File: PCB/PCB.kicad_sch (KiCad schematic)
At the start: 14 parts, among them P1 SEN-11574, SW1 SW_Push, SW2 SW_Push, SW3 SW_Push, U1 TinyS3_Symbol, U2 ADXL343, U3 ST7789V

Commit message: Custom footprints and sch update with footprints
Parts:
- removed C2: 0.1u, symbol Device:C
- removed SW1, SW2, SW3: SW_Push, symbol Switch:SW_Push
- added R4, R5, R6, R7, R8: 220, Resistor_SMD:R_0402_1005Metric_Pad0.72x0.64mm_HandSolder, symbol Device:R
- added U4: switch3, symbol custom:switch3
- BT1: value LiPO 3.7V 1200 mAh -> LiPO 3.7V 1200 mAh
- C1, C3: footprint (none) -> Capacitor_SMD:C_0402_1005Metric_Pad0.74x0.62mm_HandSolder
- P1: footprint SEN-11574:XDCR_SEN-11574 -> footprints:Heart_headers
- R1, R2, R3: footprint (none) -> Resistor_SMD:R_0402_1005Metric_Pad0.72x0.64mm_HandSolder
- U1: footprint (none) -> footprints:TinyS3D_headers
- U2: footprint Package_LGA:LGA-14_3x5mm_P0.8mm_LayoutBorder1x6y -> footprints:ADXL345_header
- U3: footprint (none) -> footprints:LCD_header
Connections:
- net BTN1: now also U4. (BTN3)
- net BTN2: now also U4. (BTN3)
- net BTN3: now also U4. (BTN3)
- net CLK: now also R5.1; no longer U3. (VCC)
- net CS: now also R6.1; no longer U3. (VCC)
- net DC: now also R7.1; no longer U3. (VCC)
- net DIN: now also R4.1; no longer U3. (VCC)
- net GND: now also U1.2 (GND), U4. (BTN3)
- net RST: now also R8.1; no longer U3. (VCC)
- new net: R7.2, U3. (GND)
- new net: R8.2, U3. (GND)
- new net: R6.2, U3. (GND)
- new net: R4.2, U3. (GND)
- new net: R5.2, U3. (GND)
- no-connect marks 15 -> 14
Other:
- moved on the sheet: U1

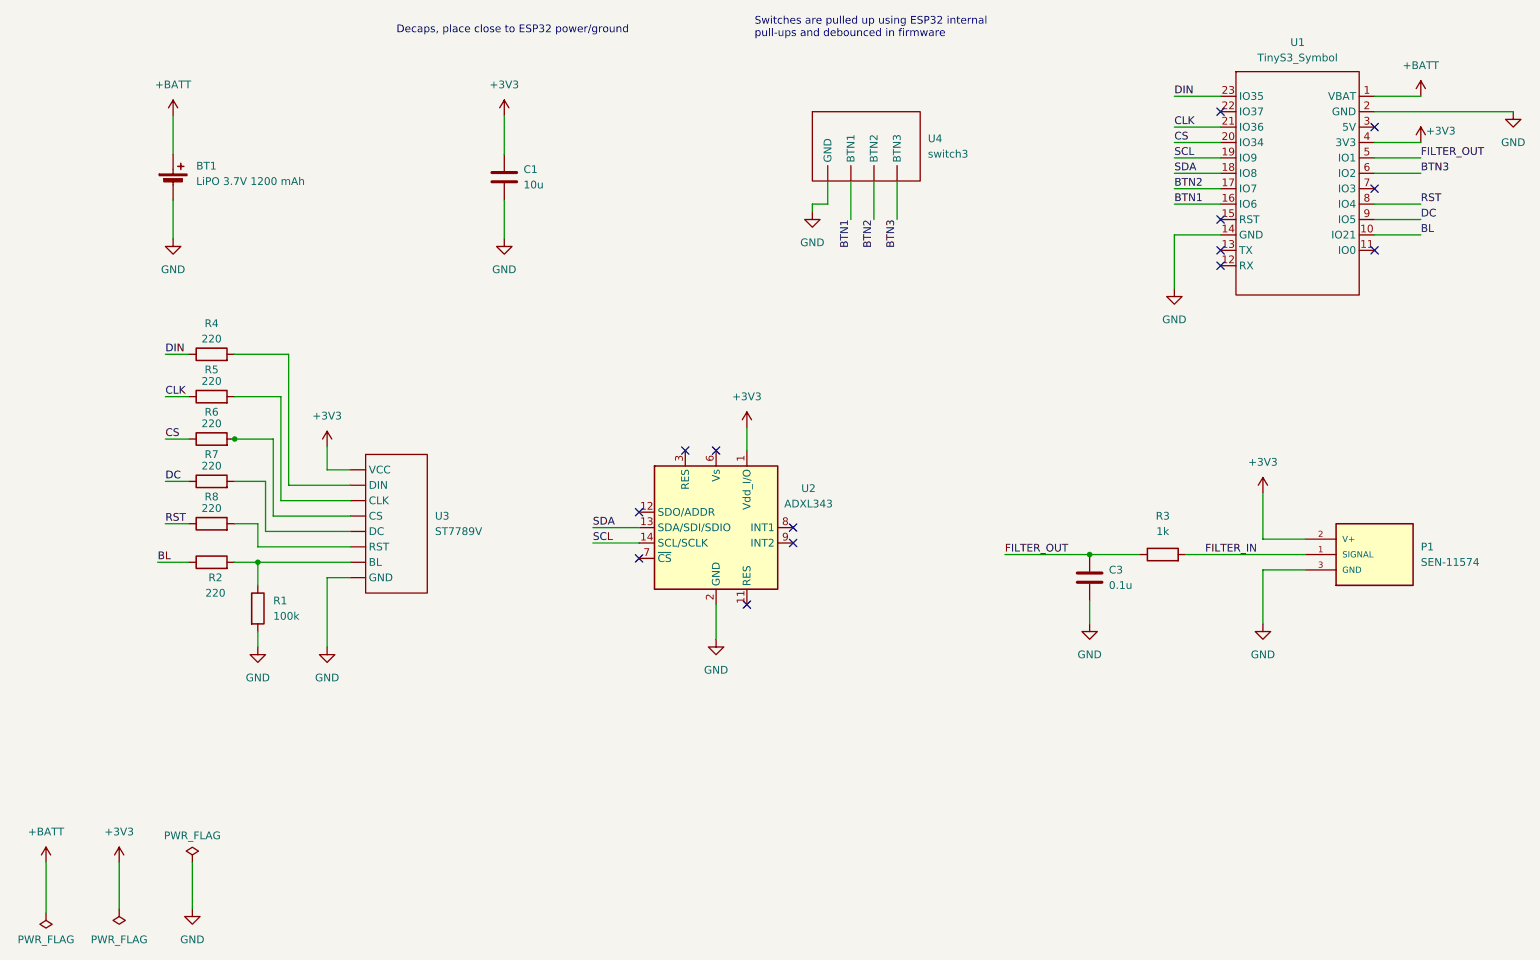
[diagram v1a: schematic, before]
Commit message: Sch rev3, fixed pin numbers to match footprints
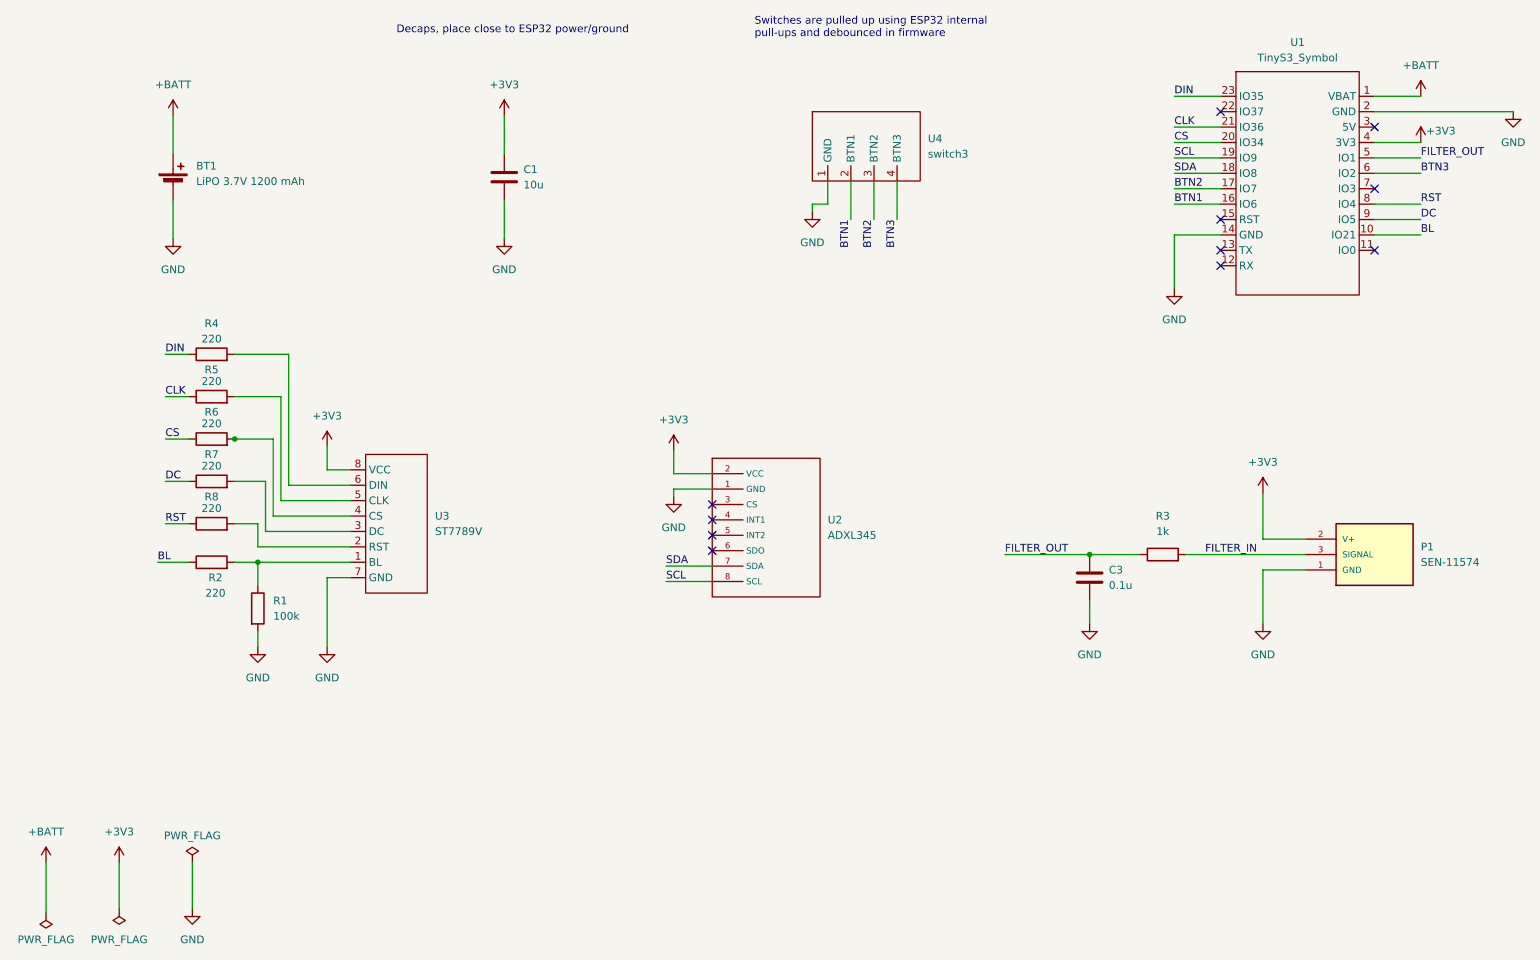
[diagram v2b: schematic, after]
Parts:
- removed U2: ADXL343, footprints:ADXL345_header, symbol Sensor_Motion:ADXL343
- added U2: ADXL345, footprints:ADXL345_header, symbol custom:ADXL345
- BT1: now left out of the parts list
- U4: footprint (none) -> footprints:Buttons_header
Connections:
- net +3V3: now also U3.8 (VCC), U2.2 (VCC); no longer U3. (GND)
- net BTN1: now also U4.2 (BTN1); no longer U4. (BTN3)
- net BTN2: now also U4.3 (BTN2); no longer U4. (BTN3)
- net BTN3: now also U4.4 (BTN3); no longer U4. (BTN3)
- net FILTER_IN: now also P1.3 (SIGNAL); no longer P1.1 (SIGNAL)
- net GND: now also P1.1 (GND), U3.7 (GND), U4.1 (GND), U2.1 (GND); no longer P1.3 (GND), U3. (GND), U4. (BTN3)
- net SCL: now also U2.8 (SCL)
- net SDA: now also U2.7 (SDA)
- net at R7.2: now also U3.3 (DC); no longer U3. (GND)
- net at R1.1, R2.2: now also U3.1 (BL); no longer U3. (GND)
- net at R8.2: now also U3.2 (RST); no longer U3. (GND)
- net at R6.2: now also U3.4 (CS); no longer U3. (GND)
- net at R4.2: now also U3.6 (DIN); no longer U3. (GND)
- net at R5.2: now also U3.5 (CLK); no longer U3. (GND)
- no-connect marks 14 -> 11

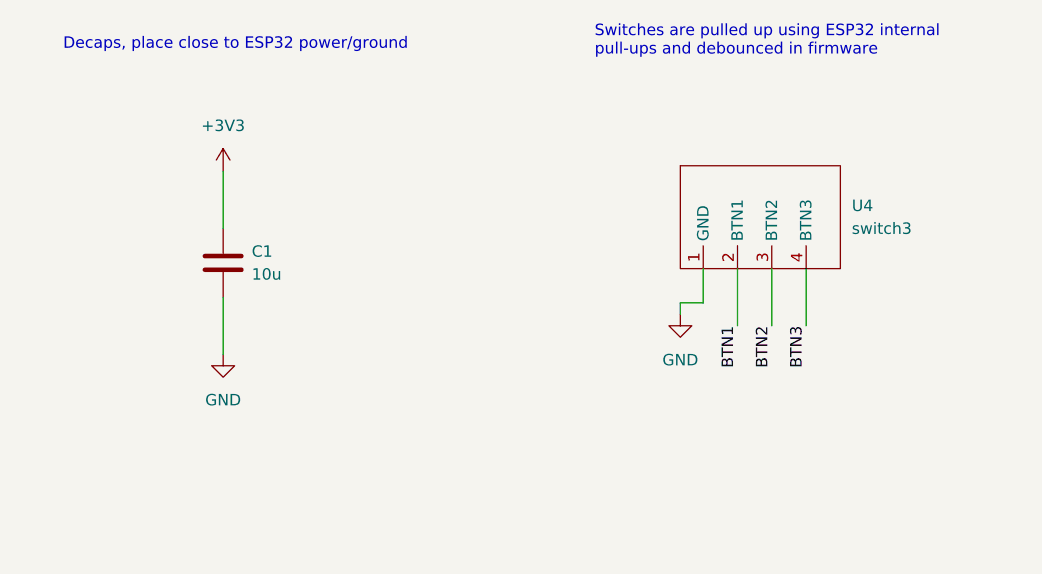
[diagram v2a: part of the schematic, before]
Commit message: PCB routed and DRC clean
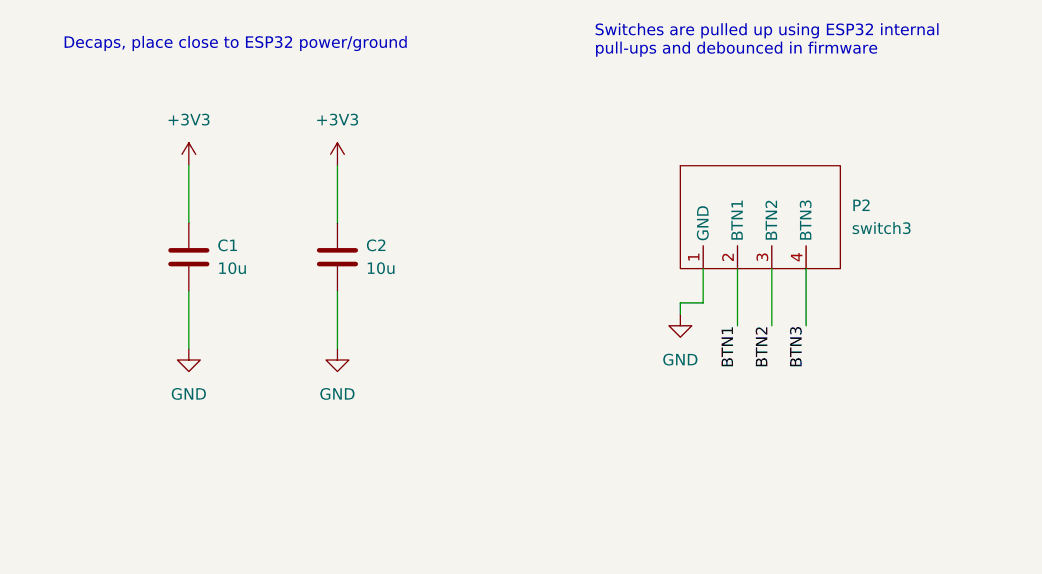
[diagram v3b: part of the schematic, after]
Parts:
- added C2: 10u, Capacitor_SMD:C_0402_1005Metric_Pad0.74x0.62mm_HandSolder, symbol Device:C
- renumbered U4 to P2
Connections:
- net +3V3: now also C2.1
- net GND: now also C2.2
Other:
- moved on the sheet: C1

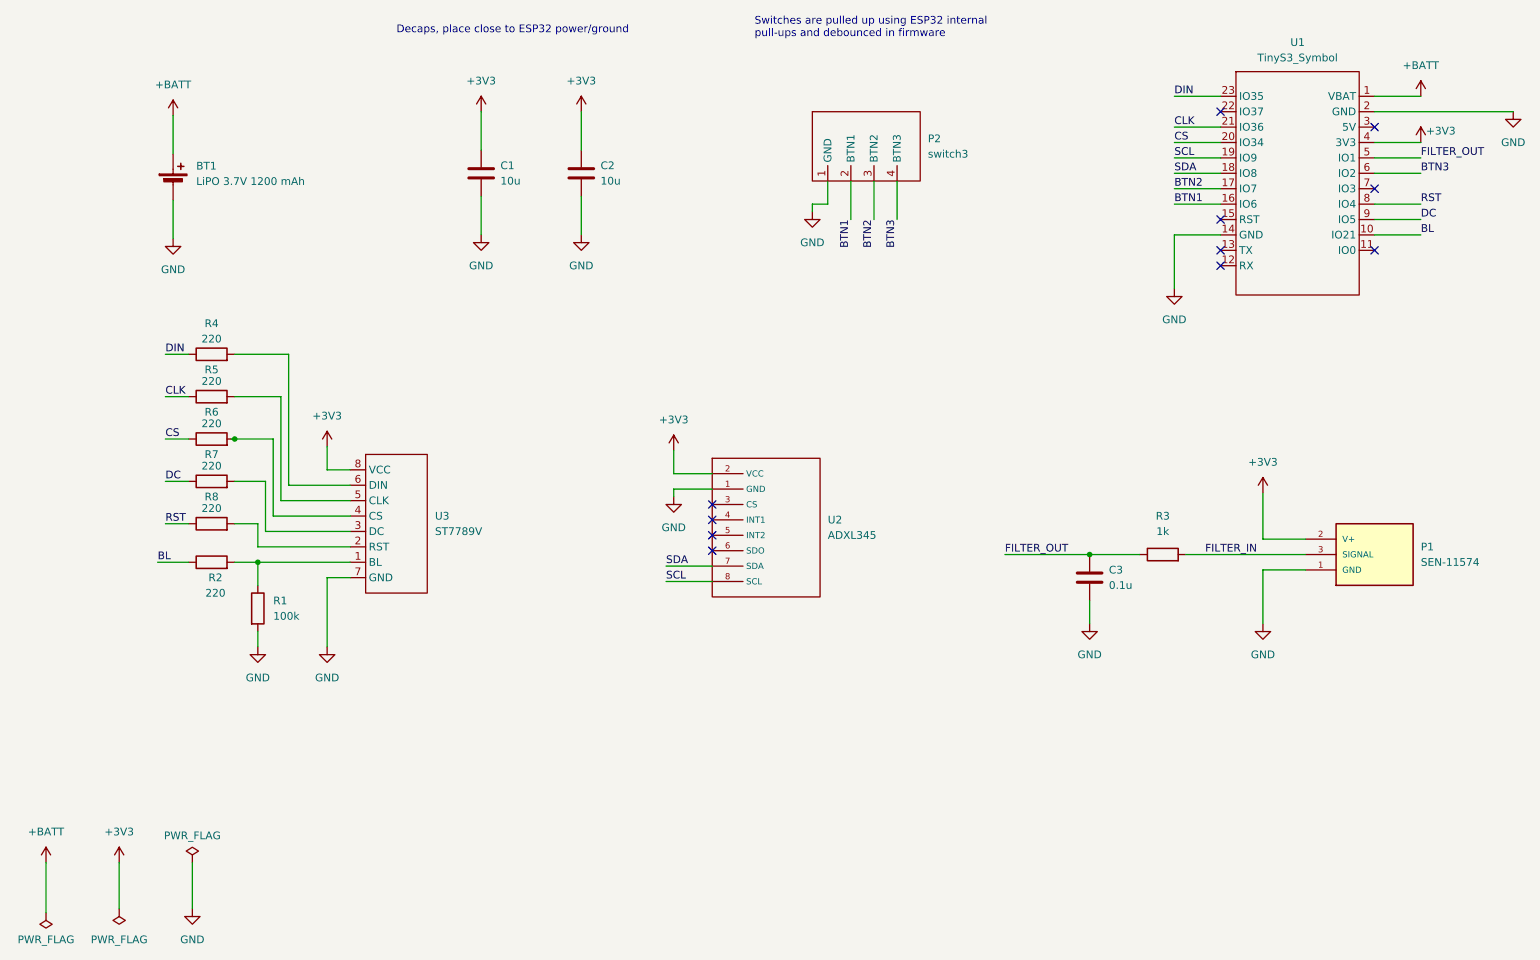
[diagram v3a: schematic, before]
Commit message: Added battery soldering pads
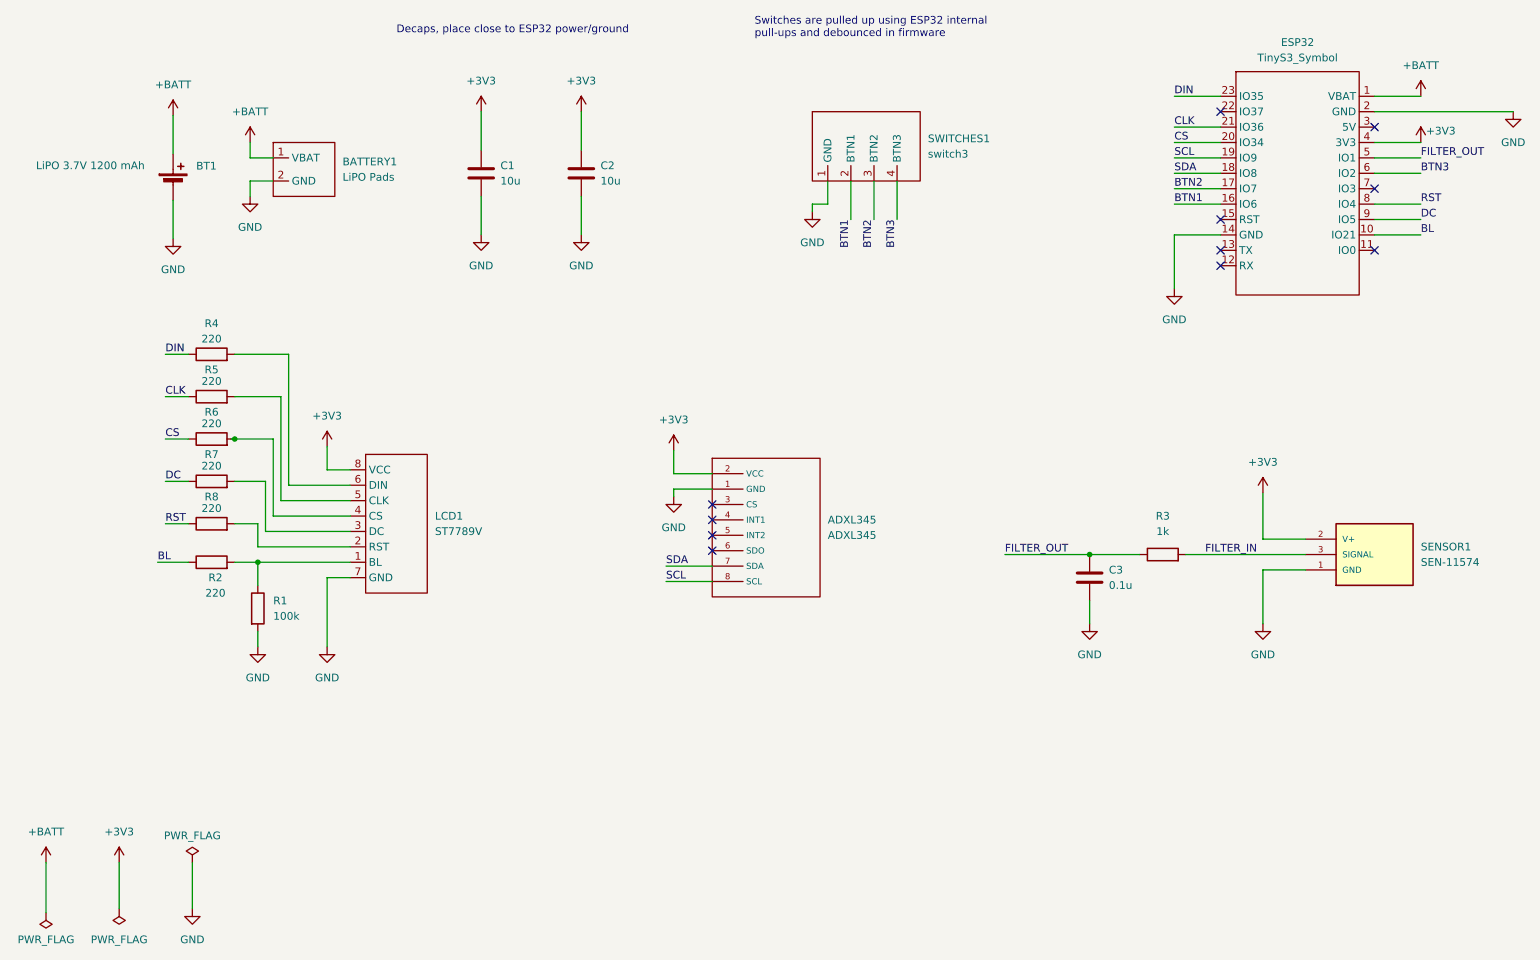
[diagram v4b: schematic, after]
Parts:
- added BATTERY1: LiPO Pads, footprints:Battery_pads, symbol custom:Battery_pads
- renumbered U2 to ADXL345, U1 to ESP32, U3 to LCD1, P1 to SENSOR1, P2 to SWITCHES1
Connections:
- net +BATT: now also BATTERY1.1 (VBAT)
- net GND: now also BATTERY1.2 (GND)

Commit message: Most recent PCB revisions, after fixing header width
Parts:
- ADXL345, BATTERY1, ESP32, LCD1, SENSOR1, SWITCHES1: now left out of the parts list
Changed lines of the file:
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@@
 		(unit 1)
 		(exclude_from_sim no)
-		(in_bom yes)
+		(in_bom no)
 		(on_board yes)
 		(dnp no)
@@
 		(unit 1)
 		(exclude_from_sim no)
-		(in_bom yes)
+		(in_bom no)
 		(on_board yes)
 		(dnp no)
@@
 		(unit 1)
 		(exclude_from_sim no)
-		(in_bom yes)
+		(in_bom no)
 		(on_board yes)
 		(dnp no)
@@
 		(unit 1)
 		(exclude_from_sim no)
-		(in_bom yes)
+		(in_bom no)
 		(on_board yes)
 		(dnp no)
@@
 		(unit 1)
 		(exclude_from_sim no)
-		(in_bom yes)
+		(in_bom no)
 		(on_board yes)
 		(dnp no)
@@
 		(unit 1)
 		(exclude_from_sim no)
-		(in_bom yes)
-		(on_board yes)
-		(dnp no)
+		(in_bom no)
+		(on_board yes)
+		(dnp no)
